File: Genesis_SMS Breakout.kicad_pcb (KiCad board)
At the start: 2 copper layers, 15 parts, among them J1 Conn_01x09_Female, J2 Conn_01x08_Female, J3 AudioJack3_SwitchTR, J4 AudioJack3_SwitchTR, J5 Conn_01x09_Female, J6 DB15_Female_HighDensity_Mount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

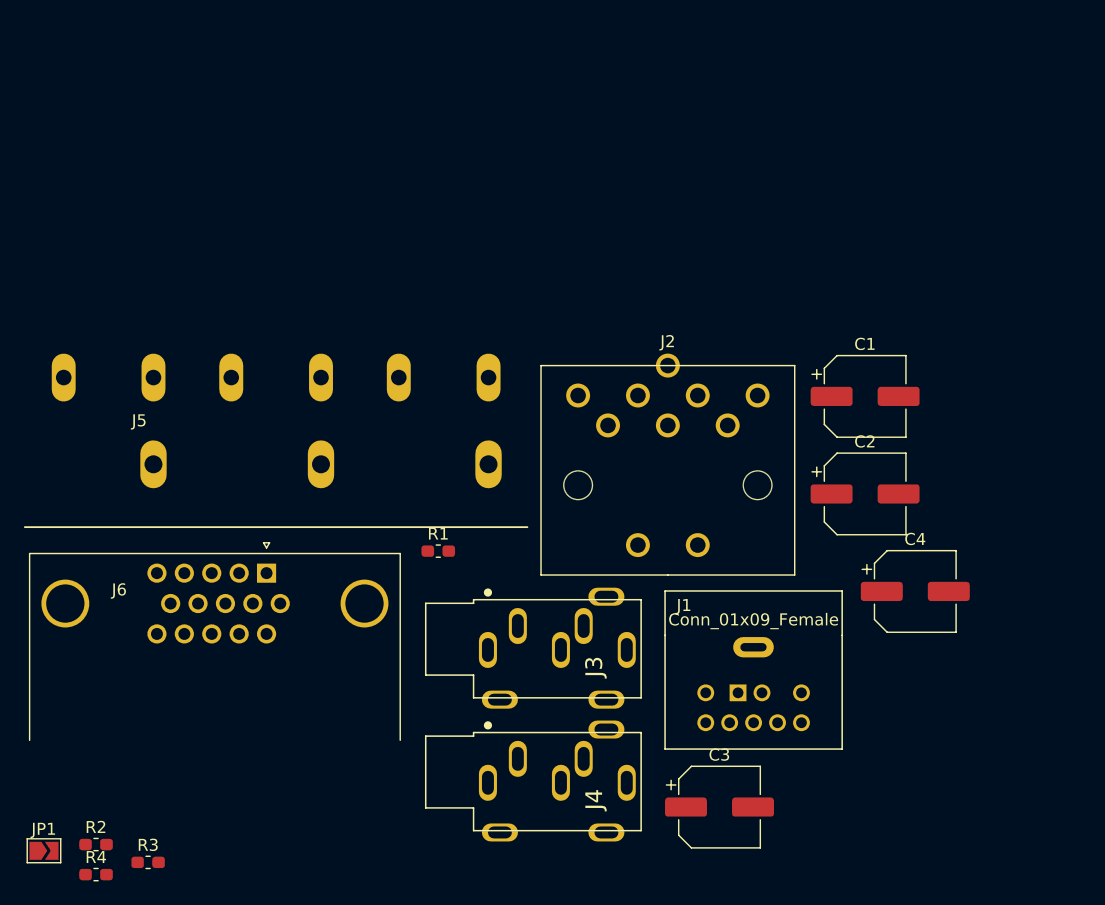
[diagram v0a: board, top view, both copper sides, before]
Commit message: Finished layout
finished PCB design, generated gerbers and renders
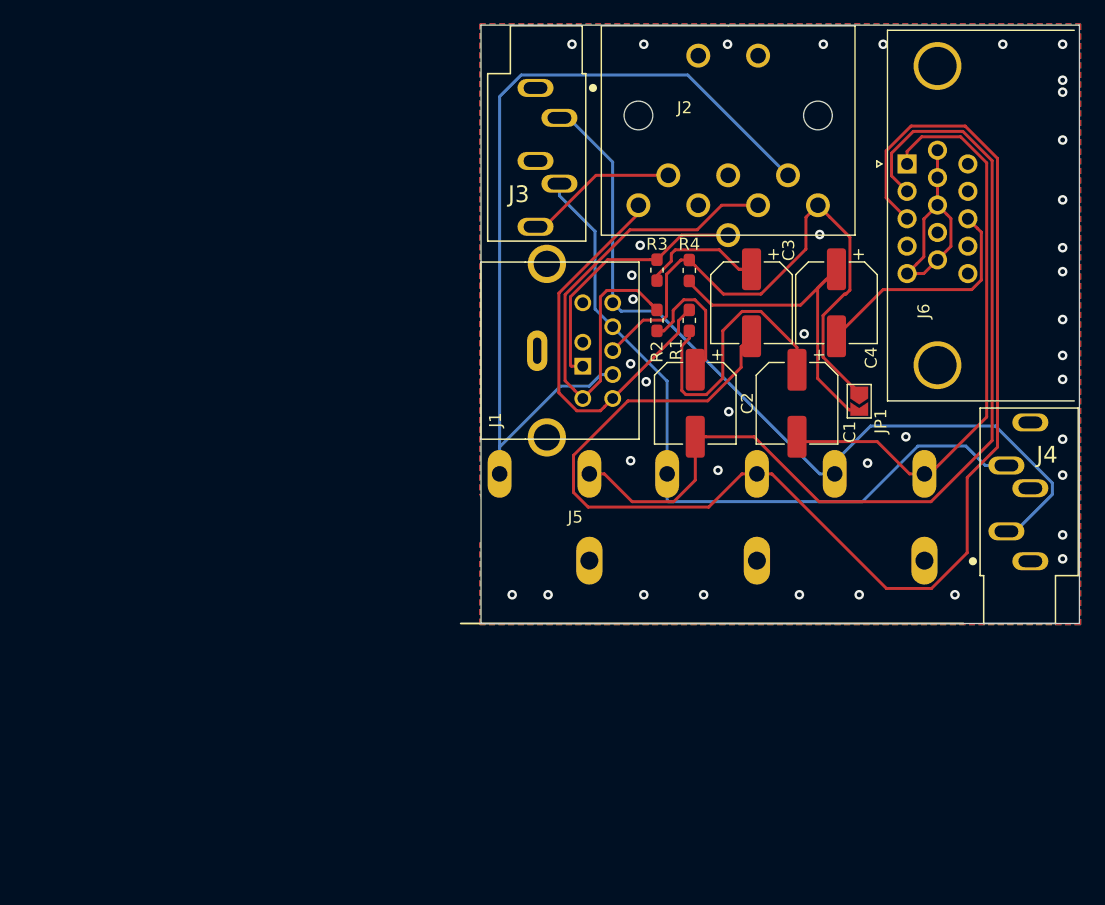
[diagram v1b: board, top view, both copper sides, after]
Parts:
- added REF**: OSHW-Logo2_14.6x12mm_SilkScreen, Symbol:OSHW-Logo2_14.6x12mm_SilkScreen, B.Cu at (160.6, 74.7)
- moved JP1 77.8 mm to (169.0, 76.8), turned to 270 degrees
- moved R4 70.8 mm to (154.8, 65.9), turned to 90 degrees
- moved R3 65.3 mm to (152.1, 65.9), turned to 90 degrees
- moved R2 64.2 mm to (152.1, 70.1), turned to 90 degrees
- moved J6 63.5 mm to (173.0, 57.0), turned to 90 degrees
- moved J4 49.0 mm to (183.3, 90.2), turned to 90 degrees
- moved J3 47.1 mm to (141.9, 50.6), turned to 270 degrees
- moved C3 42.2 mm to (160.0, 68.6), turned to 270 degrees
- moved J5 37.3 mm to (156.7, 95.4)
- moved J1 30.7 mm to (142.1, 72.6), turned to 90 degrees
- moved R1 28.5 mm to (154.8, 70.1), turned to 90 degrees
- moved C4 25.0 mm to (167.1, 68.6), turned to 270 degrees
- moved J2 16.7 mm to (158.1, 60.5), turned to 180 degrees
- moved C2 16.1 mm to (155.3, 77.0), turned to 270 degrees
- moved C1 5.72 mm to (163.8, 77.0), turned to 270 degrees
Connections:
- J1 pad S1: (no net) -> GND
- J2 pad 0: (no net) -> GND
- J2 pad 8: CYSNC -> CSYNC
- J3 pad TS: (no net) -> MONO
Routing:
- net BLUE_OUT: track 0.00 -> 114.6 mm
- net GREEN_OUT: track 0.00 -> 80.6 mm
- net CVBS: track 0.00 -> 71.8 mm
- net RIGHT: track 0.00 -> 70.7 mm
- net LEFT: track 0.00 -> 61.2 mm
- net RED_OUT: track 0.00 -> 49.5 mm
- net CSYNC: track 0.00 -> 47.2 mm
- net GREEN: track 0.00 -> 43.2 mm
- net RED: track 0.00 -> 34.0 mm
- net Net-(C4-Pad1): track 0.00 -> 27.6 mm
- net Net-(C1-Pad1): track 0.00 -> 23.8 mm
- net BLUE: track 0.00 -> 22.1 mm
- net GND: track 0.00 -> 19.9 mm, vias 0 -> 39
- net VGA_SYNC_OUT: track 0.00 -> 19.6 mm
- net MONO: track 0.00 -> 12.9 mm
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- added copper zone on B.Cu, net GND
- added copper zone on F.Cu, net GND
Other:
- board outline added: 50 x 50 mm
- board text added: "Genesis Breakout 0.1 Tinkerplunk.com"
